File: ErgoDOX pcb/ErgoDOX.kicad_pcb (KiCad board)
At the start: 2 copper layers, 182.8 x 158.9 mm, 77 parts, among them J1 USB, J2 3.5mm, J3 JMP, J4 JMP, SW0:10 SW0:3, SW0:11 SW0:2, SW0:12 SW0:1, SW0:7 SW0:6, SW0:8 SW0:5, SW0:9 SW0:4, SW1:10 SW1:3, SW1:11 SW1:2, SW1:12 SW1:1, SW1:13 SW1:0, SW1:9 SW1:4, SW2:10 SW2:3, SW2:11 SW2:2, SW2:12 SW2:1, SW2:13 SW2:0, SW2:7 SW2:6, SW2:8 SW2:5, SW2:9 SW2:4, SW3:10 SW3:3, SW3:11 SW3:2, SW3:12 SW3:1, SW3:13 SW3:0, SW3:8 SW3:5, SW3:9 SW3:4, SW4:10 SW4:3, SW4:11 SW4:2, SW4:12 SW4:1, SW4:13 SW4:0, SW4:7 SW4:6, SW4:8 SW4:5, SW4:9 SW4:4, SW5:10 SW5:3, SW5:11 SW5:2, SW5:12 SW5:1, SW5:13 SW5:0, SW5:7 SW5:6, SW5:8 SW5:5, SW5:9 SW5:4, U1 TEENSY2.0, U2 MCP23018

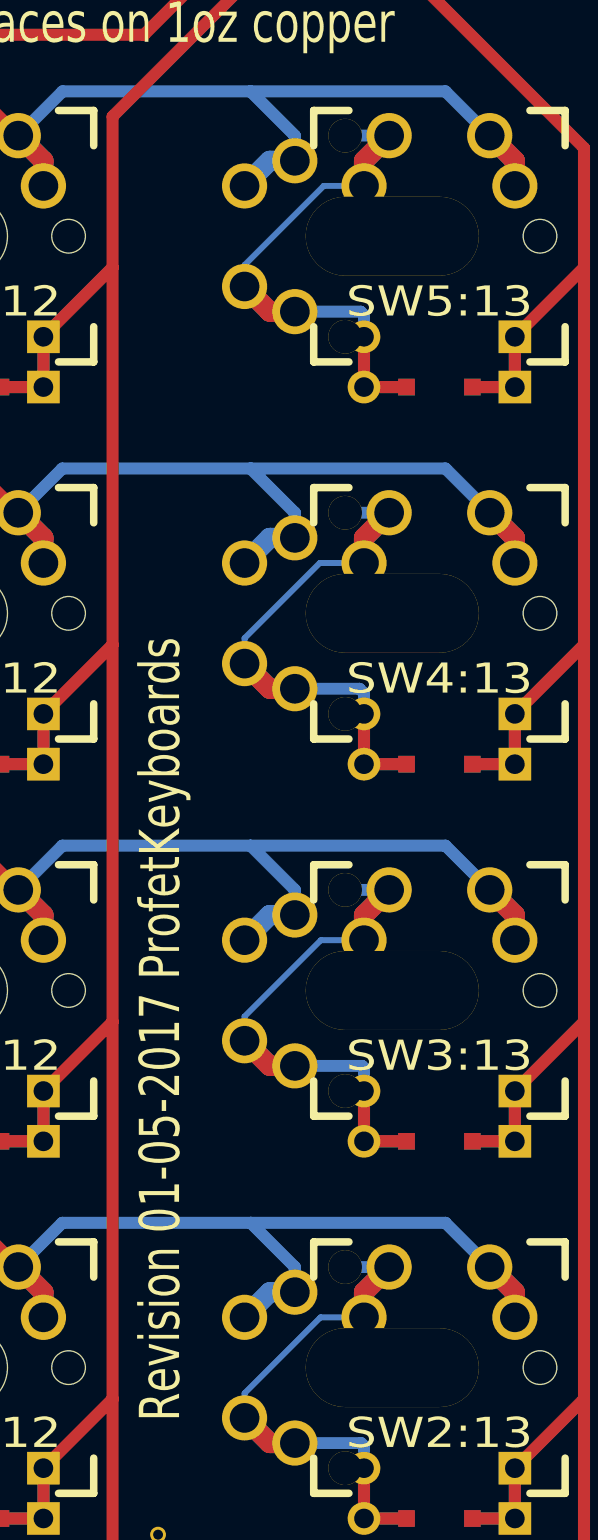
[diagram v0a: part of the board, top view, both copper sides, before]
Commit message: Update Revision and change three PTH to NPTH
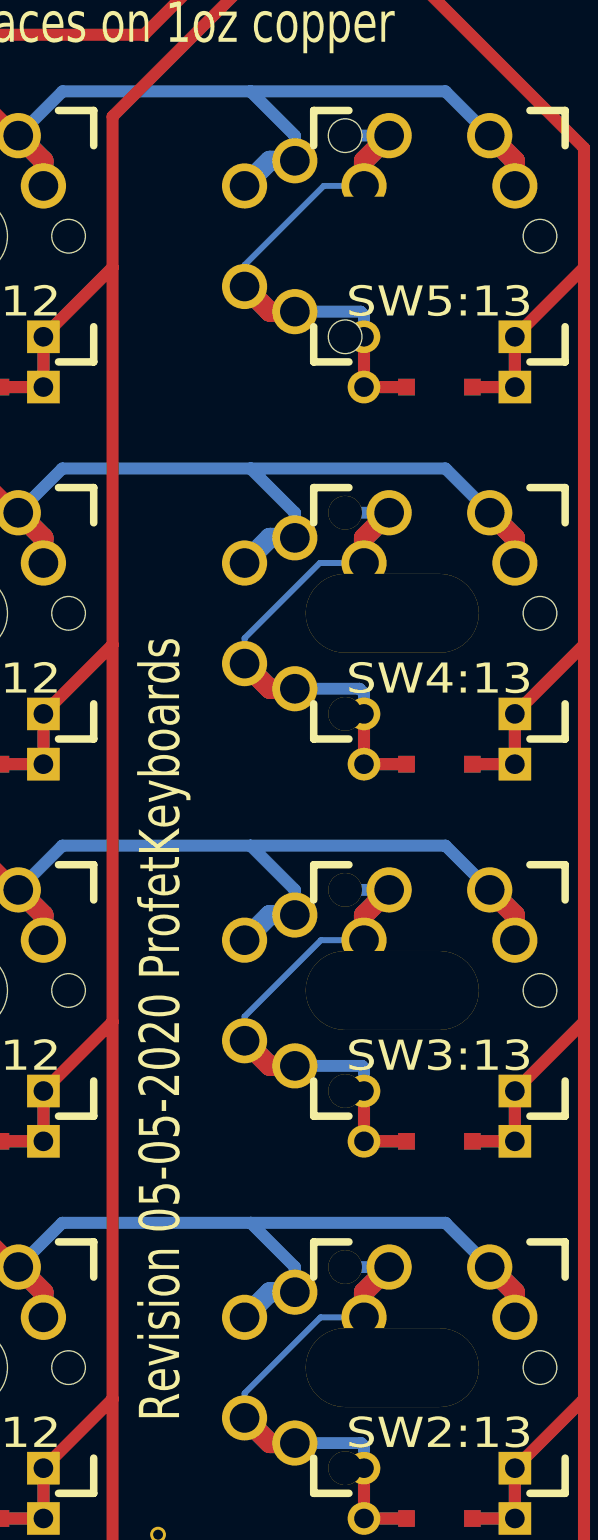
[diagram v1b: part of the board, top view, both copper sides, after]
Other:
- board text added: "Revision 05-05-2020 ProfetKeyboards"
- board text removed: "Revision 01-05-2017 ProfetKeyboards"
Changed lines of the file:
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@@
-(kicad_pcb (version 20160815) (host pcbnew "(2016-12-22 revision d365dc5)-makepkg")
+(kicad_pcb (version 20171130) (host pcbnew 5.1.5)
   (general
-    (links 384)
-    (no_connects 1)
-    (area 22.890479 27.985719 206.108301 189.542421)
     (thickness 1.6002)
     (drawings 41)
@@
   (page A4)
   (layers
-    (0 Front signal hide)
-    (31 Back signal hide)
-    (32 B.Adhes user)
-    (33 F.Adhes user)
-    (34 B.Paste user)
-    (35 F.Paste user)
+    (0 Front signal)
+    (31 Back signal)
+    (32 B.Adhes user hide)
+    (33 F.Adhes user hide)
+    (34 B.Paste user hide)
+    (35 F.Paste user hide)
     (36 B.SilkS user hide)
-    (37 F.SilkS user)
-    (38 B.Mask user)
-    (39 F.Mask user)
-    (40 Dwgs.User user)
-    (41 Cmts.User user)
-    (42 Eco1.User user)
-    (43 Eco2.User user)
-    (44 Edge.Cuts user)
+    (37 F.SilkS user hide)
+    (38 B.Mask user hide)
+    (39 F.Mask user hide)
+    (40 Dwgs.User user hide)
+    (41 Cmts.User user hide)
+    (42 Eco1.User user hide)
+    (43 Eco2.User user hide)
+    (44 Edge.Cuts user hide)
   )
   (setup
@@
     (zone_45_only yes)
     (trace_min 0.0254)
-    (segment_width 0.3048)
-    (edge_width 0.381)
     (via_size 0.6096)
     (via_drill 0.508)
@@
     (uvia_min_size 0.508)
     (uvia_min_drill 0.127)
+    (edge_width 0.381)
+    (segment_width 0.3048)
     (pcb_text_width 0.3048)
     (pcb_text_size 1.524 2.032)
@@
     (mod_text_size 1.524 1.524)
     (mod_text_width 0.3048)
-    (pad_size 0.8 0.8)
-    (pad_drill 0.5)
+    (pad_size 8.7503 3.9878)
+    (pad_drill 8.7503)
     (pad_to_mask_clearance 0.2032)
     (aux_axis_origin 0 0)
@@
       (layerselection 0x01fff_ffffffff)
       (usegerberextensions true)
+      (usegerberattributes false)
+      (usegerberadvancedattributes false)
+      (creategerberjobfile false)
       (excludeedgelayer true)
       (linewidth 0.150000)
@@
       (hpglpennumber 1)
       (hpglpenspeed 20)
-      (hpglpendiameter 100)
+      (hpglpendiameter 100.000000)
       (psnegative false)
       (psa4output false)
@@
       (drillshape 0)
       (scaleselection 1)
-      (outputdirectory gerber/))
+      (outputdirectory "gerber/"))
   )
   (net 0 "")
@@
     (uvia_dia 0.508)
     (uvia_drill 0.127)
-    (diff_pair_gap 0.25)
-    (diff_pair_width 0.2)
     (add_net /COL0)
     (add_net /COL1)
@@
     (pad 2 thru_hole circle (at -9.8425 2.54) (size 2.28092 2.28092) (drill 1.4986) (layers *.Cu *.Mask)
       (net 68 "Net-(SW5:13-Pad2)"))
-    (pad 2 thru_hole oval (at -2.38252 0) (size 8.7503 3.9878) (drill oval 8.7503 3.9878) (layers *.Cu *.Mask)
-      (net 68 "Net-(SW5:13-Pad2)") (zone_connect 2))
-    (pad 3 thru_hole circle (at -4.7625 5.08 90) (size 1.7018 1.7018) (drill 1.7018) (layers *.Cu *.Mask)
-      (net 68 "Net-(SW5:13-Pad2)") (zone_connect 2))
-    (pad 2 thru_hole circle (at -4.7625 -5.08 90) (size 1.7018 1.7018) (drill 1.7018) (layers *.Cu *.Mask)
-      (net 68 "Net-(SW5:13-Pad2)") (zone_connect 2))
+    (pad "" np_thru_hole oval (at -2.38252 0) (size 8.7503 3.9878) (drill oval 8.7503 3.9878) (layers *.Cu *.Mask)
+      (zone_connect 2))
+    (pad "" np_thru_hole circle (at -4.7625 5.08 90) (size 1.7018 1.7018) (drill 1.7018) (layers *.Cu *.Mask)
+      (zone_connect 2))
+    (pad "" np_thru_hole circle (at -4.7625 -5.08 90) (size 1.7018 1.7018) (drill 1.7018) (layers *.Cu *.Mask)
+      (zone_connect 2))
   )
   (module "ErgoDOX pcb:MX_FLIP_XX" (layer Front)
@@
     (effects (font (size 2.032 1.524) (thickness 0.3048)))
   )
-  (gr_text "Revision 01-05-2017 ProfetKeyboards" (at 177.36 126.86 90) (layer F.SilkS)
+  (gr_text "Revision 05-05-2020 ProfetKeyboards" (at 177.36 126.86 90) (layer F.SilkS)
     (effects (font (size 2.032 1.524) (thickness 0.3048)) (justify left))
   )
